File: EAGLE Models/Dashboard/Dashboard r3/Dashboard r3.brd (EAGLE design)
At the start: 105.5 x 67.2 mm, 69 parts, among them IC1 AT90CAN128, IC2 MCP2551SO8, IC3 NUP2105L, Q1 56P2859, U1 74LCX125M

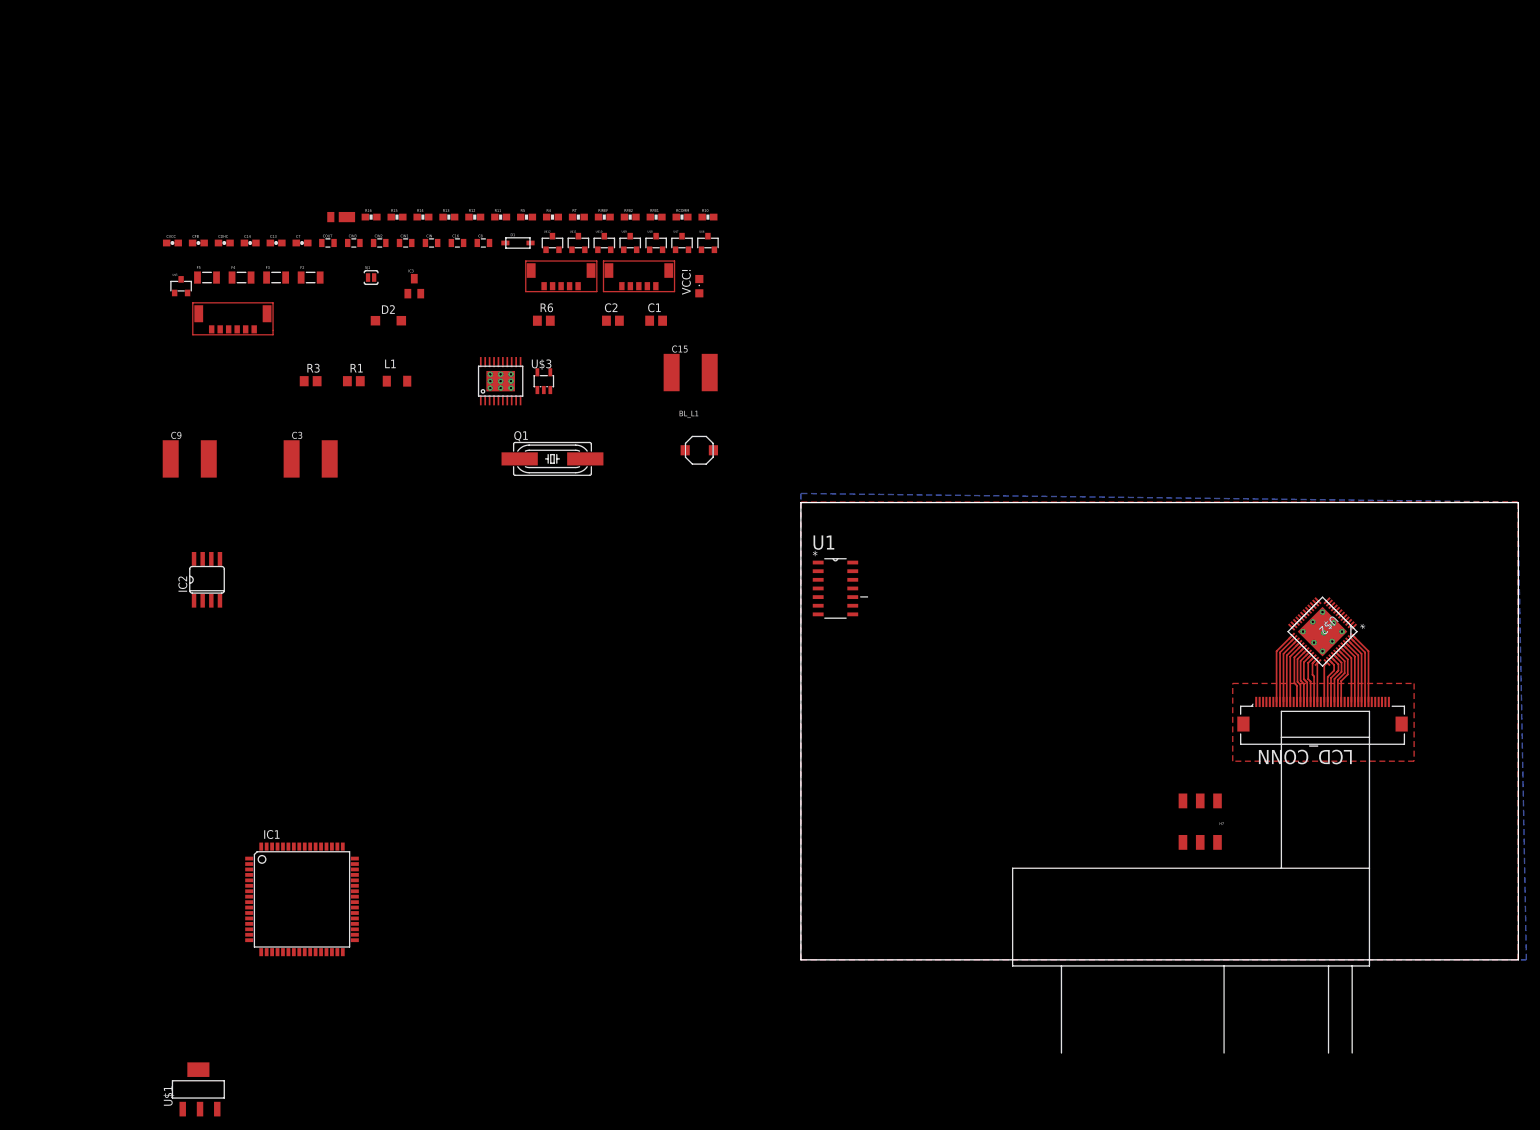
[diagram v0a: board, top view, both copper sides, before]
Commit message: forgot save: moved all board components into blocks for easier routing
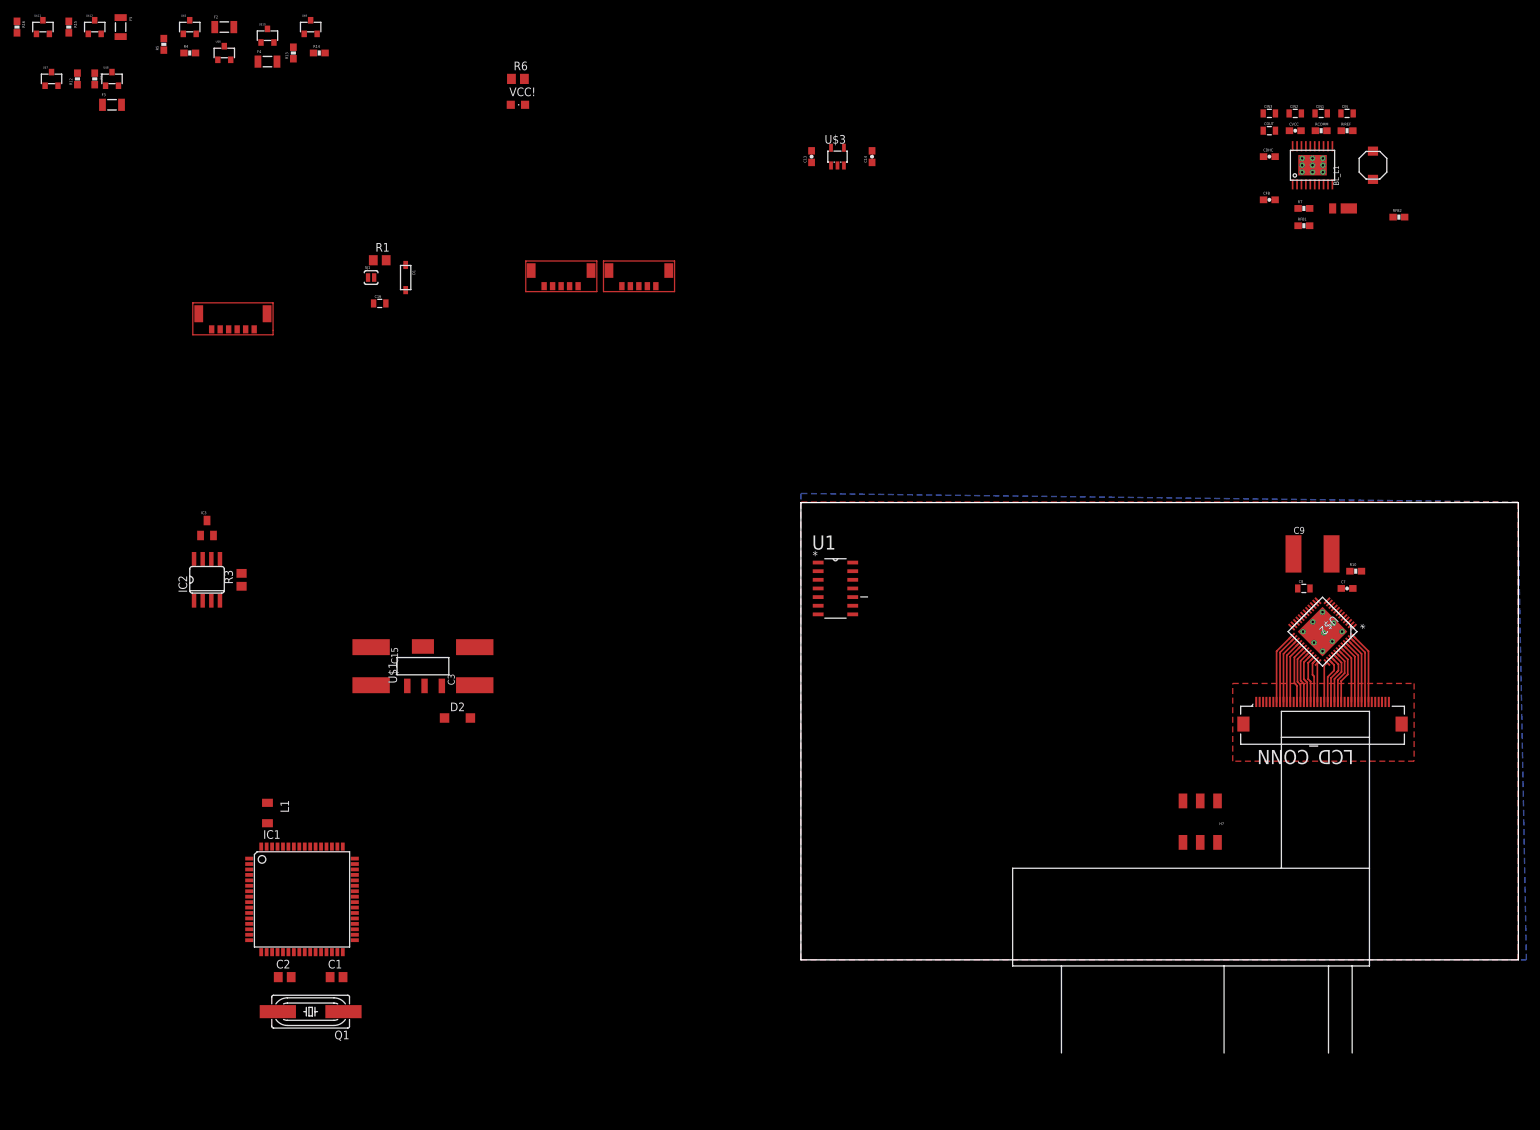
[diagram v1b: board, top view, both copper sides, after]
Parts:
- moved CVCC 165.9 mm to (71.1, 121.9)
- moved C9 165.7 mm to (73.7, 59.7)
- moved C7 161.8 mm to (78.7, 54.6)
- moved CFB 157.6 mm to (67.3, 111.8)
- moved CDHC 154.2 mm to (67.3, 118.1)
- moved BL_D1 147.3 mm to (77.5, 110.5)
- moved COUT 139.4 mm to (67.3, 121.9)
- moved CIN 136.0 mm to (78.7, 124.5)
- moved CIN1 136.0 mm to (74.9, 124.5)
- moved CIN2 136.0 mm to (71.1, 124.5)
- moved CIN3 136.0 mm to (67.3, 124.5)
- moved C8 130.9 mm to (72.4, 54.6)
- moved U$4 123.5 mm to (73.7, 116.8)
- moved RFB2 113.0 mm to (86.4, 109.2)
- moved RIREF 110.0 mm to (78.7, 121.9)
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
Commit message: Began placing components on the board
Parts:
- added H1, H2, H3, H4: MOUNT-PAD-ROUND#4-40-PAD, holes:#4-40-PAD-ROUND
- CANPWR, LEDOUT: value MICRO5LOCK -> (none); device DashAndCAN library:MICRO5LOCK -> molex:43650-0513
- moved IC3 144.2 mm to (47.0, 15.2), turned to 180 degrees
- moved IC2 139.8 mm to (47.0, 22.9), turned to 180 degrees
- moved R3 130.0 mm to (41.9, 22.9), turned to 270 degrees
- moved C16 128.3 mm to (45.7, 29.2)
- moved D1 128.3 mm to (49.5, 33.0)
- moved R1 128.3 mm to (45.7, 35.6)
- moved SJ1 128.3 mm to (44.5, 33.0)
- moved IC1 122.1 mm to (40.6, 48.3)
- moved L1 114.1 mm to (27.9, 58.4), turned to 0 degrees
- moved C2 113.1 mm to (21.6, 52.1), turned to 90 degrees
- moved Q1 106.8 mm to (16.5, 49.5), turned to 90 degrees
- moved C1 104.0 mm to (21.6, 47.0), turned to 270 degrees
- moved C15 86.9 mm to (20.3, 25.4)
- moved C3 86.9 mm to (35.6, 25.4)
- moved D2 86.9 mm to (33.0, 17.8)
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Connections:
- net 12V: now also CANPWR.2; no longer CANPWR.P2
- net CAN_H: now also CANPWR.4; no longer CANPWR.P4
- net CAN_L: now also CANPWR.3; no longer CANPWR.P3
- net DRV1: now also LEDOUT.2; no longer LEDOUT.P2
- net DRV2: now also LEDOUT.3; no longer LEDOUT.P3
- net DRV3: now also LEDOUT.4; no longer LEDOUT.P4
- net GND: now also CANPWR.1, LEDOUT.1; no longer CANPWR.P1, LEDOUT.P1
- net VCC: now also CANPWR.5; no longer CANPWR.P5

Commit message: continued placing components on dashboard
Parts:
- ROT/PUSH: value MICRO6LOCK -> (none); device DashAndCAN library:MICRO6LOCK -> molex:43650-0513-7
- moved R16 236.4 mm to (92.7, 27.7)
- moved U$7 232.7 mm to (89.2, 12.2), turned to 270 degrees
- moved R12 232.3 mm to (92.7, 12.4), turned to 270 degrees
- moved R11 232.0 mm to (92.7, 8.89)
- moved R15 231.4 mm to (92.7, 24.1)
- moved F3 230.4 mm to (95.2, 8.13), turned to 90 degrees
- moved U$11 230.0 mm to (89.2, 27.4), turned to 270 degrees
- moved F5 227.2 mm to (95.2, 23.6), turned to 90 degrees
- moved U$8 227.1 mm to (89.2, 8.38), turned to 270 degrees
- moved U$12 225.1 mm to (89.2, 23.9), turned to 270 degrees
- moved R5 220.1 mm to (92.7, 20.1), turned to 270 degrees
- moved F2 218.3 mm to (95.2, 16.0), turned to 90 degrees
- moved R4 218.1 mm to (92.7, 16.5), turned to 270 degrees
- moved U$5 215.2 mm to (89.2, 20.1), turned to 270 degrees
- moved U$6 210.8 mm to (89.2, 16.5), turned to 270 degrees
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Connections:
- net GND: now also ROT/PUSH.4; no longer ROT/PUSH.P4
- net PC0: now also ROT/PUSH.1; no longer ROT/PUSH.P1
- net PF0: now also ROT/PUSH.5; no longer ROT/PUSH.P5
- net PF1: now also ROT/PUSH.3; no longer ROT/PUSH.P3
- net PF2: now also ROT/PUSH.2; no longer ROT/PUSH.P2
- net VCC: now also ROT/PUSH.6; no longer ROT/PUSH.P6
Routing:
- net BL_CATHODE: track 0.00 -> 31.2 mm
- net BL_ANODE: track 0.00 -> 30.0 mm
- net 12V: track 0.00 -> 19.2 mm
- net N$10: track 0.00 -> 16.5 mm
- net GND: track 5.83 -> 21.5 mm
- net N$8: track 0.00 -> 14.5 mm
- net N$12: track 0.00 -> 7.28 mm
- net N$38: track 0.00 -> 6.91 mm
- net N$42: track 0.00 -> 6.22 mm
- net N$26: track 0.00 -> 6.17 mm
- net N$30: track 0.00 -> 5.92 mm
- net N$4: track 0.00 -> 5.83 mm
- net N$23: track 0.00 -> 5.80 mm
- net N$27: track 0.00 -> 5.70 mm
- net N$39: track 0.00 -> 5.70 mm
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- removed copper zone on layer 1, net N$15

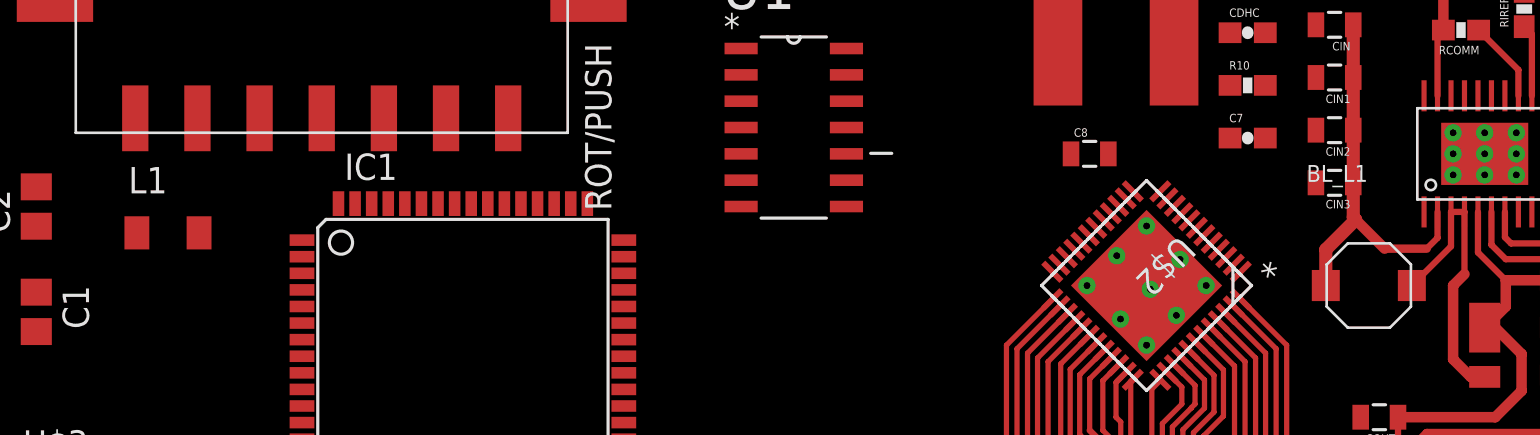
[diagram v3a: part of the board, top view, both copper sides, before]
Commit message: Deleted reference boxes and moved some stuff around
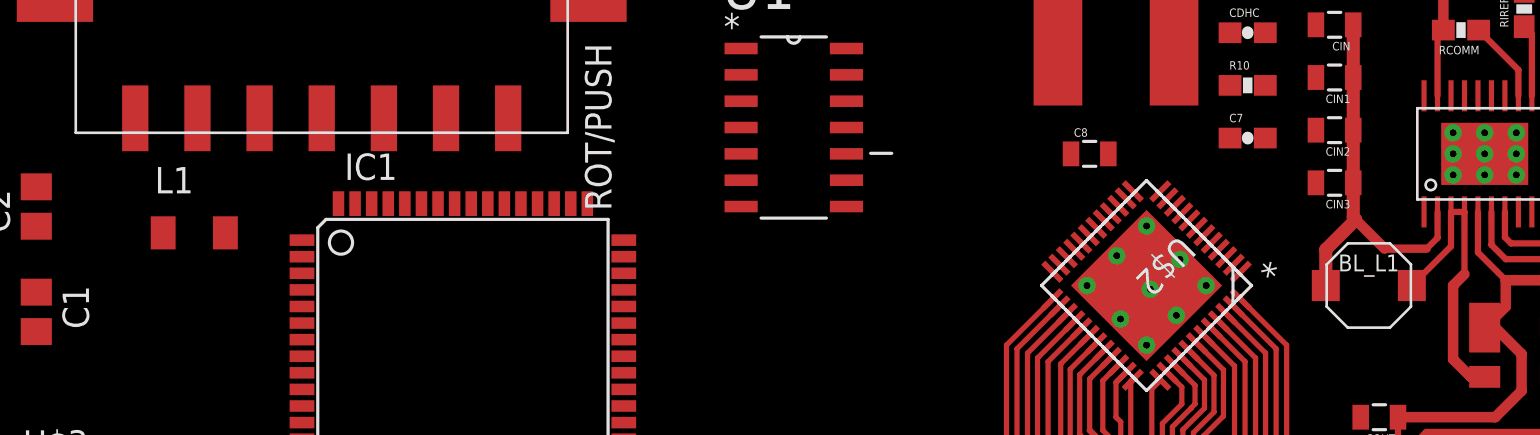
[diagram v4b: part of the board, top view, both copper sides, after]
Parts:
- moved L1 1.27 mm to (29.2, 50.8)

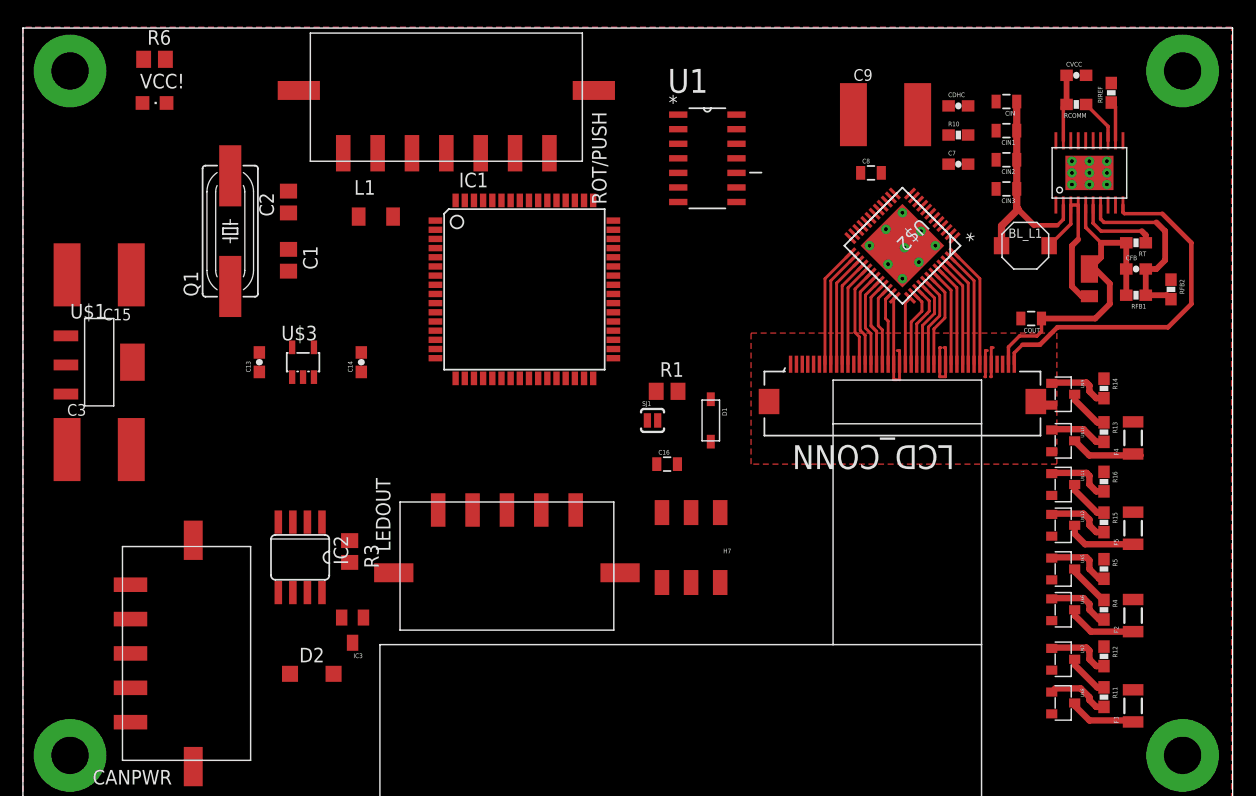
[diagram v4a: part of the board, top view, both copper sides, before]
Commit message: began routing traces
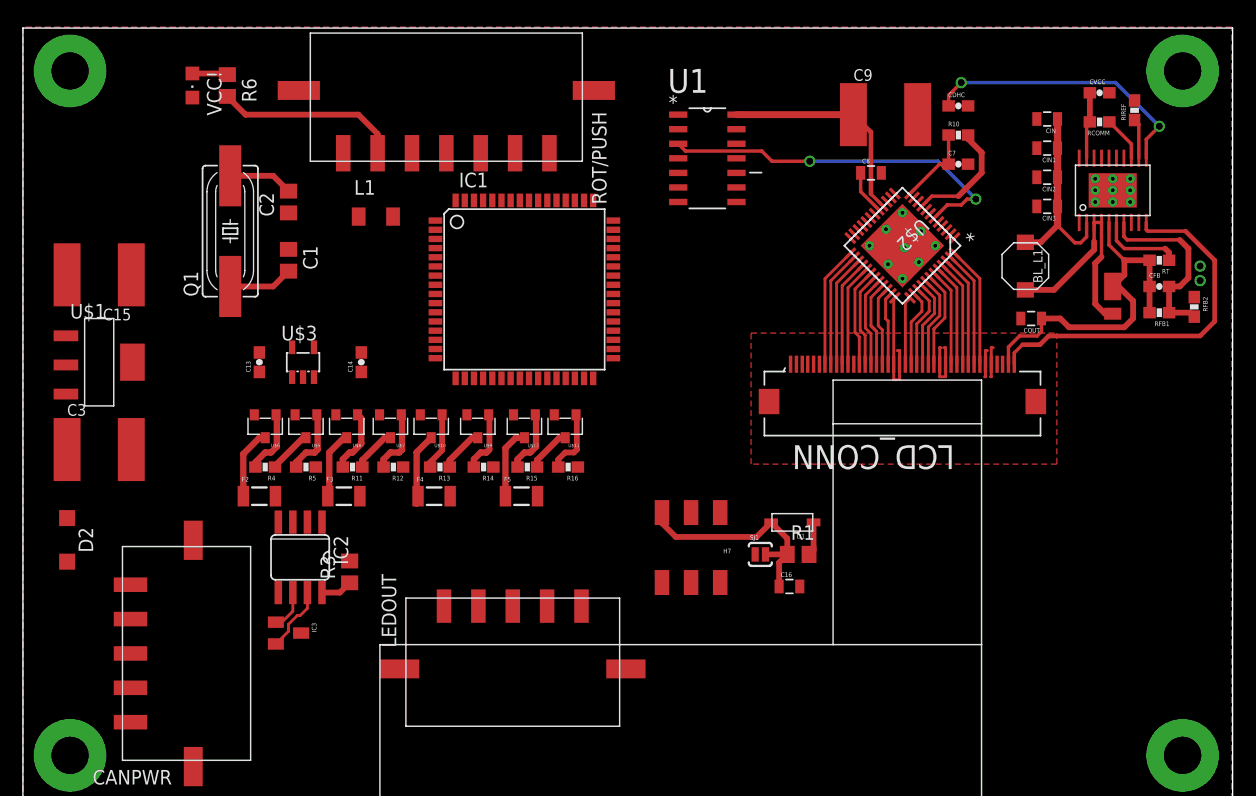
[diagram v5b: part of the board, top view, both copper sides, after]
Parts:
- moved F2 76.9 mm to (19.1, 26.4), turned to 0 degrees
- moved R4 74.2 mm to (19.6, 29.0), turned to 180 degrees
- moved U$6 71.4 mm to (19.6, 32.5), turned to 180 degrees
- moved F3 71.2 mm to (26.4, 26.4), turned to 0 degrees
- moved R5 70.2 mm to (23.1, 29.0), turned to 180 degrees
- moved R11 68.5 mm to (27.2, 29.0), turned to 180 degrees
- moved U$5 67.2 mm to (23.1, 32.5), turned to 180 degrees
- moved U$8 67.0 mm to (26.7, 32.5), turned to 180 degrees
- moved R12 64.1 mm to (30.7, 29.0), turned to 180 degrees
- moved U$7 62.1 mm to (30.5, 32.5), turned to 180 degrees
- moved F4 61.2 mm to (34.3, 26.4), turned to 0 degrees
- moved R13 58.0 mm to (34.8, 29.0), turned to 180 degrees
- moved U$10 55.1 mm to (34.0, 32.5), turned to 180 degrees
- moved R14 54.5 mm to (38.6, 29.0), turned to 180 degrees
- moved F5 53.4 mm to (41.9, 26.4), turned to 0 degrees
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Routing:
- net FT801_CS_N: track 0.00 -> 32.2 mm, vias 0 -> 2
- net 3.3V: track 0.00 -> 29.4 mm
- net N$7: track 0.00 -> 24.6 mm, vias 0 -> 2
- net RESET: track 0.00 -> 19.8 mm
- net VCC: track 0.00 -> 19.1 mm
- net N$3: track 0.00 -> 6.97 mm
- net CAN_H: track 0.00 -> 5.77 mm
- net XTAL1: track 0.00 -> 5.63 mm
- net N$11: track 0.00 -> 5.63 mm
- net N$8: track 14.5 -> 20.0 mm
- net N$2: track 0.00 -> 3.86 mm
- net CAN_L: track 0.00 -> 3.50 mm
- net N$9: track 0.00 -> 3.09 mm
- net N$6: track 0.00 -> 2.77 mm
- net BL_ANODE: track 30.0 -> 31.9 mm
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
